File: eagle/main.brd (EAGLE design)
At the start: 98.7 x 90.2 mm, 31 parts, among them IC1 7805TV, U1 INA213AIDCKT, U2 LM1117MP-3.3, U3 INA213AIDCKT, U4 INA213AIDCKT

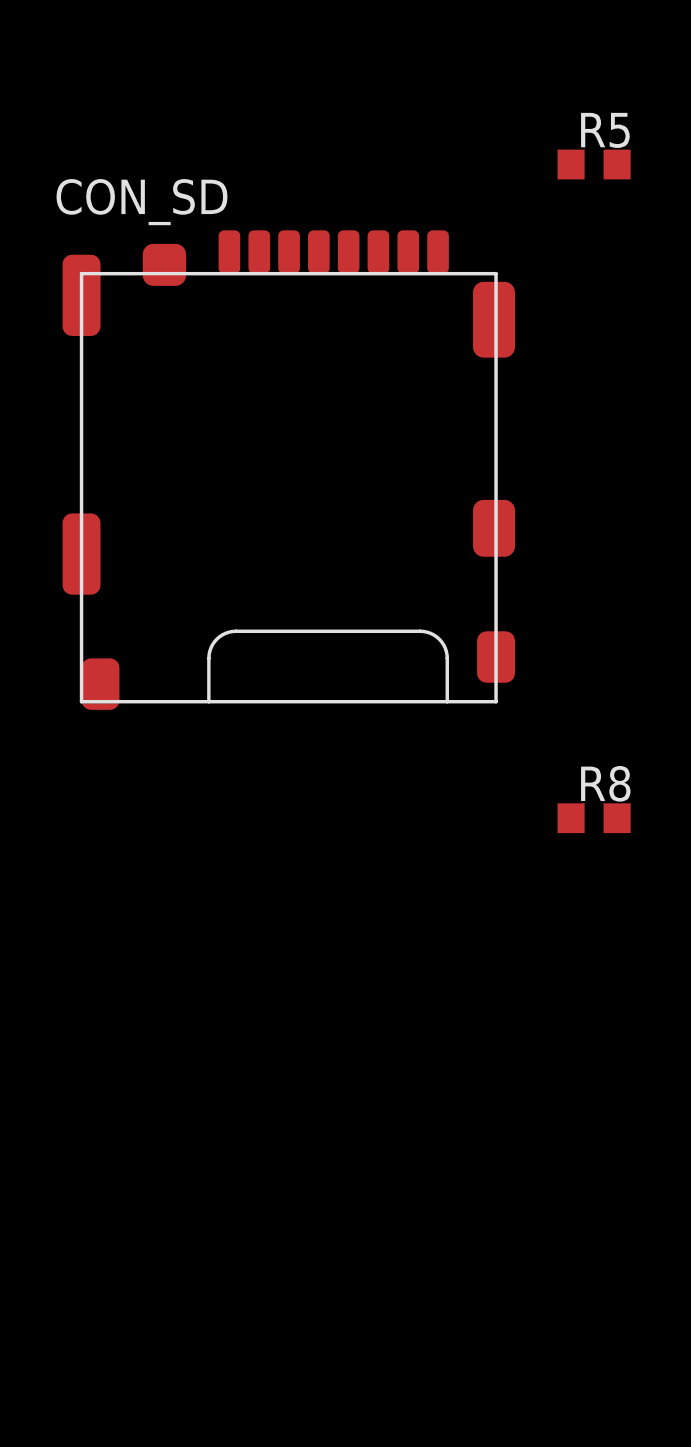
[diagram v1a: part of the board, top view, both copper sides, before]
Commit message: add Spansion flash memory
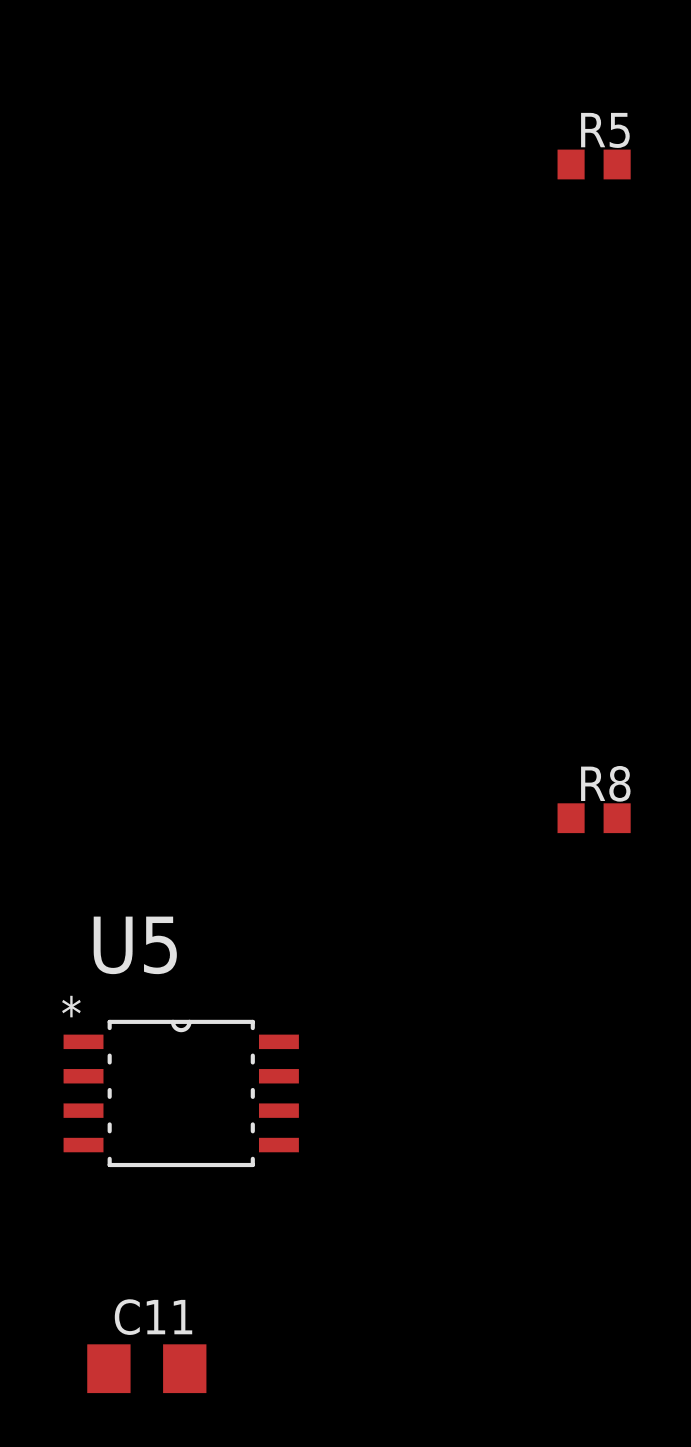
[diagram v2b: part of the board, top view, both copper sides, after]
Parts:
- removed CON_SD: MICROSD_SPI_MODE, con-molex-microsd:MICRO_SD_CONNECTOR
- added C11: 100n, rcl:C1206
- added U5: S25FL064K0SMFI011, Spansion_By_element14_Batch_1:SOIC127P800X215-8N
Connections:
- new net FLASH_CSN: U5.1
- new net FLASH_MISO: U5.2
- new net FLASH_MOSI: U5.5
- new net FLASH_SCK: U5.6
- net DC_3V3: now also C11.1, U5.8
- net GND: now also C11.2, U5.4
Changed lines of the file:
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@@
 <element name="C9" library="rcl" package="C1206" value="100n" x="-59.69" y="-68.58"/>
 <element name="C10" library="rcl" package="C1206" value="100n" x="-53.34" y="-68.58"/>
-<element name="CON_SD" library="con-molex-microsd" package="MICRO_SD_CONNECTOR" value="MICROSD_SPI_MODE" x="-81.28" y="-62.23"/>
+<element name="U5" library="Spansion_By_element14_Batch_1" package="SOIC127P800X215-8N" value="S25FL064K0SMFI011" x="-85.09" y="-85.09">
+<attribute name="PACKAGE" value="SOIC-8" x="-85.09" y="-85.09" size="1.778" layer="27" display="off"/>
+<attribute name="OC_NEWARK" value="27T2974" x="-85.09" y="-85.09" size="1.778" layer="27" display="off"/>
+<attribute name="MPN" value="S25FL064K0SMFI011" x="-85.09" y="-85.09" size="1.778" layer="27" display="off"/>
+<attribute name="SUPPLIER" value="SPANSION" x="-85.09" y="-85.09" size="1.778" layer="27" display="off"/>
+<attribute name="OC_FARNELL" value="1861631" x="-85.09" y="-85.09" size="1.778" layer="27" display="off"/>
+</element>
+<element name="C11" library="rcl" package="C1206" value="100n" x="-86.36" y="-95.25"/>
 </elements>
 <signals>
@@
 <contactref element="U4" pad="2"/>
 <contactref element="C10" pad="2"/>
-<wire x1="63.5" y1="78.74" x2="29.4386" y2="53.9496" width="0" layer="19" extent="1-1"/>
+<contactref element="U5" pad="4"/>
+<contactref element="C11" pad="2"/>
+<wire x1="-88.6968" y1="-86.995" x2="-84.96" y2="-95.25" width="0" layer="19" extent="1-1"/>
+<wire x1="-64.35" y1="-74.93" x2="-88.6968" y2="-86.995" width="0" layer="19" extent="1-1"/>
+<wire x1="-58.29" y1="-68.58" x2="-64.35" y2="-74.93" width="0" layer="19" extent="1-1"/>
+<wire x1="-51.94" y1="-68.58" x2="-58.29" y2="-68.58" width="0" layer="19" extent="1-1"/>
+<wire x1="-64.35" y1="-50.8" x2="-58.29" y2="-68.58" width="0" layer="19" extent="1-1"/>
+<wire x1="-58.29" y1="-44.45" x2="-64.35" y2="-50.8" width="0" layer="19" extent="1-1"/>
+<wire x1="-51.94" y1="-44.45" x2="-58.29" y2="-44.45" width="0" layer="19" extent="1-1"/>
+<wire x1="-65.81" y1="-25.4" x2="-58.29" y2="-44.45" width="0" layer="19" extent="1-1"/>
+<wire x1="-65.81" y1="-17.78" x2="-65.81" y2="-25.4" width="0" layer="19" extent="1-1"/>
+<wire x1="-56.92" y1="-10.16" x2="-65.81" y2="-17.78" width="0" layer="19" extent="1-1"/>
+<wire x1="-56.92" y1="-3.81" x2="-56.92" y2="-10.16" width="0" layer="19" extent="1-1"/>
+<wire x1="6.35" y1="17.78" x2="-56.92" y2="-3.81" width="0" layer="19" extent="1-1"/>
+<wire x1="6.35" y1="27.94" x2="6.35" y2="17.78" width="0" layer="19" extent="1-1"/>
+<wire x1="18.0086" y1="20.32" x2="6.35" y2="17.78" width="0" layer="19" extent="1-1"/>
+<wire x1="18.0086" y1="20.9804" x2="18.0086" y2="20.32" width="0" layer="19" extent="1-1"/>
+<wire x1="6.35" y1="43.18" x2="6.35" y2="27.94" width="0" layer="19" extent="1-1"/>
+<wire x1="6.35" y1="53.34" x2="6.35" y2="43.18" width="0" layer="19" extent="1-1"/>
+<wire x1="18.0086" y1="45.72" x2="6.35" y2="43.18" width="0" layer="19" extent="1-1"/>
+<wire x1="18.0086" y1="46.3804" x2="18.0086" y2="45.72" width="0" layer="19" extent="1-1"/>
+<wire x1="20.32" y1="57.15" x2="18.0086" y2="46.3804" width="0" layer="19" extent="1-1"/>
+<wire x1="29.4386" y1="53.9496" x2="20.32" y2="57.15" width="0" layer="19" extent="1-1"/>
+<wire x1="6.35" y1="68.58" x2="6.35" y2="53.34" width="0" layer="19" extent="1-1"/>
+<wire x1="6.35" y1="78.74" x2="6.35" y2="68.58" width="0" layer="19" extent="1-1"/>
+<wire x1="18.0086" y1="72.39" x2="6.35" y2="68.58" width="0" layer="19" extent="1-1"/>
+<wire x1="18.0086" y1="73.0504" x2="18.0086" y2="72.39" width="0" layer="19" extent="1-1"/>
+<wire x1="30.61" y1="73.66" x2="18.0086" y2="73.0504" width="0" layer="19" extent="1-1"/>
+<wire x1="-18.63" y1="74.93" x2="6.35" y2="78.74" width="0" layer="19" extent="1-1"/>
+<wire x1="-46.86" y1="73.66" x2="-18.63" y2="74.93" width="0" layer="19" extent="1-1"/>
+<wire x1="63.5" y1="78.74" x2="30.61" y2="73.66" width="0" layer="19" extent="1-1"/>
 <wire x1="71.12" y1="45.72" x2="63.5" y2="78.74" width="0" layer="19" extent="1-1"/>
-<wire x1="6.35" y1="78.74" x2="63.5" y2="78.74" width="0" layer="19" extent="1-1"/>
-<wire x1="6.35" y1="68.58" x2="6.35" y2="78.74" width="0" layer="19" extent="1-1"/>
-<wire x1="6.35" y1="53.34" x2="6.35" y2="68.58" width="0" layer="19" extent="1-1"/>
-<wire x1="6.35" y1="43.18" x2="6.35" y2="53.34" width="0" layer="19" extent="1-1"/>
-<wire x1="6.35" y1="27.94" x2="6.35" y2="43.18" width="0" layer="19" extent="1-1"/>
-<wire x1="6.35" y1="17.78" x2="6.35" y2="27.94" width="0" layer="19" extent="1-1"/>
-<wire x1="95.25" y1="66.04" x2="6.35" y2="17.78" width="0" layer="19" extent="1-1"/>
-<wire x1="-18.63" y1="74.93" x2="6.35" y2="78.74" width="0" layer="19" extent="1-1"/>
-<wire x1="18.0086" y1="20.9804" x2="-18.63" y2="74.93" width="0" layer="19" extent="1-1"/>
-<wire x1="18.0086" y1="20.32" x2="18.0086" y2="20.9804" width="0" layer="19" extent="1-1"/>
-<wire x1="20.32" y1="57.15" x2="18.0086" y2="20.32" width="0" layer="19" extent="1-1"/>
-<wire x1="30.61" y1="73.66" x2="20.32" y2="57.15" width="0" layer="19" extent="1-1"/>
-<wire x1="-46.86" y1="73.66" x2="30.61" y2="73.66" width="0" layer="19" extent="1-1"/>
-<wire x1="-56.92" y1="-3.81" x2="6.35" y2="17.78" width="0" layer="19" extent="1-1"/>
-<wire x1="-56.92" y1="-10.16" x2="-56.92" y2="-3.81" width="0" layer="19" extent="1-1"/>
-<wire x1="-65.81" y1="-17.78" x2="-56.92" y2="-10.16" width="0" layer="19" extent="1-1"/>
-<wire x1="-65.81" y1="-25.4" x2="-65.81" y2="-17.78" width="0" layer="19" extent="1-1"/>
-<wire x1="18.0086" y1="46.3804" x2="-65.81" y2="-25.4" width="0" layer="19" extent="1-1"/>
-<wire x1="18.0086" y1="45.72" x2="18.0086" y2="46.3804" width="0" layer="19" extent="1-1"/>
-<wire x1="-58.29" y1="-44.45" x2="18.0086" y2="45.72" width="0" layer="19" extent="1-1"/>
-<wire x1="-51.94" y1="-44.45" x2="-58.29" y2="-44.45" width="0" layer="19" extent="1-1"/>
-<wire x1="-64.35" y1="-50.8" x2="-58.29" y2="-44.45" width="0" layer="19" extent="1-1"/>
-<wire x1="18.0086" y1="73.0504" x2="-64.35" y2="-50.8" width="0" layer="19" extent="1-1"/>
-<wire x1="18.0086" y1="72.39" x2="18.0086" y2="73.0504" width="0" layer="19" extent="1-1"/>
-<wire x1="-58.29" y1="-68.58" x2="18.0086" y2="72.39" width="0" layer="19" extent="1-1"/>
-<wire x1="-51.94" y1="-68.58" x2="-58.29" y2="-68.58" width="0" layer="19" extent="1-1"/>
-<wire x1="-64.35" y1="-74.93" x2="-58.29" y2="-68.58" width="0" layer="19" extent="1-1"/>
+<wire x1="95.25" y1="66.04" x2="71.12" y2="45.72" width="0" layer="19" extent="1-1"/>
 </signal>
 <signal name="AGND">
@@
 <contactref element="U4" pad="3"/>
 <contactref element="C10" pad="1"/>
-<wire x1="18.0086" y1="19.6596" x2="34.0614" y2="53.9496" width="0" layer="19" extent="1-1"/>
-<wire x1="-49.66" y1="73.66" x2="18.0086" y2="19.6596" width="0" layer="19" extent="1-1"/>
-<wire x1="20.32" y1="52.07" x2="18.0086" y2="19.6596" width="0" layer="19" extent="1-1"/>
-<wire x1="-68.81" y1="-17.78" x2="20.32" y2="52.07" width="0" layer="19" extent="1-1"/>
-<wire x1="18.0086" y1="45.0596" x2="-68.81" y2="-17.78" width="0" layer="19" extent="1-1"/>
-<wire x1="-54.74" y1="-44.45" x2="18.0086" y2="45.0596" width="0" layer="19" extent="1-1"/>
-<wire x1="18.0086" y1="71.7296" x2="-54.74" y2="-44.45" width="0" layer="19" extent="1-1"/>
-<wire x1="-54.74" y1="-68.58" x2="18.0086" y2="71.7296" width="0" layer="19" extent="1-1"/>
+<wire x1="-54.74" y1="-44.45" x2="-54.74" y2="-68.58" width="0" layer="19" extent="1-1"/>
+<wire x1="-68.81" y1="-17.78" x2="-54.74" y2="-44.45" width="0" layer="19" extent="1-1"/>
+<wire x1="-49.66" y1="73.66" x2="-68.81" y2="-17.78" width="0" layer="19" extent="1-1"/>
+<wire x1="18.0086" y1="71.7296" x2="-49.66" y2="73.66" width="0" layer="19" extent="1-1"/>
+<wire x1="20.32" y1="52.07" x2="18.0086" y2="71.7296" width="0" layer="19" extent="1-1"/>
+<wire x1="18.0086" y1="45.0596" x2="20.32" y2="52.07" width="0" layer="19" extent="1-1"/>
+<wire x1="34.0614" y1="53.9496" x2="20.32" y2="52.07" width="0" layer="19" extent="1-1"/>
+<wire x1="18.0086" y1="19.6596" x2="18.0086" y2="45.0596" width="0" layer="19" extent="1-1"/>
 </signal>
 <signal name="PV_ISENSE">
@@
 <contactref element="U2" pad="2"/>
 <contactref element="C6" pad="+"/>
-<wire x1="31.75" y1="53.9496" x2="31.75" y2="60.3504" width="0" layer="19" extent="1-1"/>
-<wire x1="-68.81" y1="-25.4" x2="31.75" y2="53.9496" width="0" layer="19" extent="1-1"/>
+<contactref element="U5" pad="8"/>
+<contactref element="C11" pad="1"/>
+<wire x1="-81.4832" y1="-83.185" x2="-87.76" y2="-95.25" width="0" layer="19" extent="1-1"/>
+<wire x1="-68.81" y1="-25.4" x2="-81.4832" y2="-83.185" width="0" layer="19" extent="1-1"/>
+<wire x1="31.75" y1="53.9496" x2="-68.81" y2="-25.4" width="0" layer="19" extent="1-1"/>
+<wire x1="31.75" y1="60.3504" x2="31.75" y2="53.9496" width="0" layer="19" extent="1-1"/>
 </signal>
 <signal name="USB_5V">
@@
 <contactref element="U4" pad="6"/>
 </signal>
+<signal name="FLASH_SCK">
+<contactref element="U5" pad="6"/>
+</signal>
+<signal name="FLASH_MOSI">
+<contactref element="U5" pad="5"/>
+</signal>
+<signal name="FLASH_CSN">
+<contactref element="U5" pad="1"/>
+</signal>
+<signal name="FLASH_MISO">
+<contactref element="U5" pad="2"/>
+</signal>
 </signals>

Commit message: add dia
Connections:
- new net LOAD_GND: C7.2, CON_LOAD.P$3, CON_LOAD.P$4, R6.1
- new net PV_GND: C1.2, CON_PV.P$3, CON_PV.P$4, R3.1
- net GND: no longer C1.2, C7.2, CON_LOAD.P$3, CON_LOAD.P$4, CON_PV.P$3, CON_PV.P$4, R3.1, R6.1
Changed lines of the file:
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@@
 <contactref element="U$1" pad="GND1"/>
 <contactref element="CON_SPI" pad="1"/>
-<contactref element="CON_PV" pad="P$3"/>
-<contactref element="CON_LOAD" pad="P$3"/>
 <contactref element="CON_BAT" pad="P$3"/>
-<contactref element="R3" pad="1"/>
-<contactref element="C1" pad="2"/>
 <contactref element="U1" pad="1"/>
 <contactref element="U1" pad="2"/>
 <contactref element="C2" pad="2"/>
-<contactref element="CON_PV" pad="P$4"/>
-<contactref element="CON_LOAD" pad="P$4"/>
 <contactref element="CON_BAT" pad="P$4"/>
 <contactref element="IC1" pad="2"/>
@@
 <contactref element="C5" pad="-"/>
 <contactref element="C6" pad="-"/>
-<contactref element="R6" pad="1"/>
-<contactref element="C7" pad="2"/>
 <contactref element="U3" pad="1"/>
 <contactref element="U3" pad="2"/>
@@
 <wire x1="-58.29" y1="-68.58" x2="-64.35" y2="-74.93" width="0" layer="19" extent="1-1"/>
 <wire x1="-51.94" y1="-68.58" x2="-58.29" y2="-68.58" width="0" layer="19" extent="1-1"/>
-<wire x1="-64.35" y1="-50.8" x2="-58.29" y2="-68.58" width="0" layer="19" extent="1-1"/>
-<wire x1="-58.29" y1="-44.45" x2="-64.35" y2="-50.8" width="0" layer="19" extent="1-1"/>
-<wire x1="-51.94" y1="-44.45" x2="-58.29" y2="-44.45" width="0" layer="19" extent="1-1"/>
-<wire x1="-65.81" y1="-25.4" x2="-58.29" y2="-44.45" width="0" layer="19" extent="1-1"/>
+<wire x1="-51.94" y1="-44.45" x2="-51.94" y2="-68.58" width="0" layer="19" extent="1-1"/>
+<wire x1="-65.81" y1="-25.4" x2="-51.94" y2="-44.45" width="0" layer="19" extent="1-1"/>
 <wire x1="-65.81" y1="-17.78" x2="-65.81" y2="-25.4" width="0" layer="19" extent="1-1"/>
 <wire x1="-56.92" y1="-10.16" x2="-65.81" y2="-17.78" width="0" layer="19" extent="1-1"/>
 <wire x1="-56.92" y1="-3.81" x2="-56.92" y2="-10.16" width="0" layer="19" extent="1-1"/>
-<wire x1="6.35" y1="17.78" x2="-56.92" y2="-3.81" width="0" layer="19" extent="1-1"/>
-<wire x1="6.35" y1="27.94" x2="6.35" y2="17.78" width="0" layer="19" extent="1-1"/>
-<wire x1="18.0086" y1="20.32" x2="6.35" y2="17.78" width="0" layer="19" extent="1-1"/>
-<wire x1="18.0086" y1="20.9804" x2="18.0086" y2="20.32" width="0" layer="19" extent="1-1"/>
-<wire x1="6.35" y1="43.18" x2="6.35" y2="27.94" width="0" layer="19" extent="1-1"/>
-<wire x1="6.35" y1="53.34" x2="6.35" y2="43.18" width="0" layer="19" extent="1-1"/>
-<wire x1="18.0086" y1="45.72" x2="6.35" y2="43.18" width="0" layer="19" extent="1-1"/>
-<wire x1="18.0086" y1="46.3804" x2="18.0086" y2="45.72" width="0" layer="19" extent="1-1"/>
-<wire x1="20.32" y1="57.15" x2="18.0086" y2="46.3804" width="0" layer="19" extent="1-1"/>
-<wire x1="29.4386" y1="53.9496" x2="20.32" y2="57.15" width="0" layer="19" extent="1-1"/>
-<wire x1="6.35" y1="68.58" x2="6.35" y2="53.34" width="0" layer="19" extent="1-1"/>
-<wire x1="6.35" y1="78.74" x2="6.35" y2="68.58" width="0" layer="19" extent="1-1"/>
+<wire x1="-46.86" y1="73.66" x2="-56.92" y2="-3.81" width="0" layer="19" extent="1-1"/>
+<wire x1="6.35" y1="78.74" x2="-46.86" y2="73.66" width="0" layer="19" extent="1-1"/>
+<wire x1="6.35" y1="68.58" x2="6.35" y2="78.74" width="0" layer="19" extent="1-1"/>
 <wire x1="18.0086" y1="72.39" x2="6.35" y2="68.58" width="0" layer="19" extent="1-1"/>
 <wire x1="18.0086" y1="73.0504" x2="18.0086" y2="72.39" width="0" layer="19" extent="1-1"/>
-<wire x1="30.61" y1="73.66" x2="18.0086" y2="73.0504" width="0" layer="19" extent="1-1"/>
-<wire x1="-18.63" y1="74.93" x2="6.35" y2="78.74" width="0" layer="19" extent="1-1"/>
-<wire x1="-46.86" y1="73.66" x2="-18.63" y2="74.93" width="0" layer="19" extent="1-1"/>
-<wire x1="63.5" y1="78.74" x2="30.61" y2="73.66" width="0" layer="19" extent="1-1"/>
+<wire x1="20.32" y1="57.15" x2="18.0086" y2="72.39" width="0" layer="19" extent="1-1"/>
+<wire x1="29.4386" y1="53.9496" x2="20.32" y2="57.15" width="0" layer="19" extent="1-1"/>
+<wire x1="18.0086" y1="46.3804" x2="20.32" y2="57.15" width="0" layer="19" extent="1-1"/>
+<wire x1="18.0086" y1="45.72" x2="18.0086" y2="46.3804" width="0" layer="19" extent="1-1"/>
+<wire x1="18.0086" y1="20.9804" x2="18.0086" y2="45.72" width="0" layer="19" extent="1-1"/>
+<wire x1="18.0086" y1="20.32" x2="18.0086" y2="20.9804" width="0" layer="19" extent="1-1"/>
+<wire x1="63.5" y1="78.74" x2="29.4386" y2="53.9496" width="0" layer="19" extent="1-1"/>
 <wire x1="71.12" y1="45.72" x2="63.5" y2="78.74" width="0" layer="19" extent="1-1"/>
 <wire x1="95.25" y1="66.04" x2="71.12" y2="45.72" width="0" layer="19" extent="1-1"/>
@@
 <contactref element="U5" pad="2"/>
 </signal>
+<signal name="LOAD_GND">
+<contactref element="CON_LOAD" pad="P$3"/>
+<contactref element="CON_LOAD" pad="P$4"/>
+<contactref element="R6" pad="1"/>
+<contactref element="C7" pad="2"/>
+<wire x1="-58.29" y1="-44.45" x2="-64.35" y2="-50.8" width="0" layer="19" extent="1-1"/>
+<wire x1="6.35" y1="43.18" x2="-58.29" y2="-44.45" width="0" layer="19" extent="1-1"/>
+<wire x1="6.35" y1="53.34" x2="6.35" y2="43.18" width="0" layer="19" extent="1-1"/>
+</signal>
+<signal name="PV_GND">
+<contactref element="CON_PV" pad="P$3"/>
+<contactref element="CON_PV" pad="P$4"/>
+<contactref element="R3" pad="1"/>
+<contactref element="C1" pad="2"/>
+<wire x1="-18.63" y1="74.93" x2="30.61" y2="73.66" width="0" layer="19" extent="1-1"/>
+<wire x1="6.35" y1="27.94" x2="30.61" y2="73.66" width="0" layer="19" extent="1-1"/>
+<wire x1="6.35" y1="17.78" x2="6.35" y2="27.94" width="0" layer="19" extent="1-1"/>
+</signal>
 </signals>

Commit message: add TI library
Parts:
- removed C10, C9: 100n, rcl:C1206
- removed CON_SPI: (no value), con-lstb:MA06-1
- removed R7: 0.002, resistor:R2512
- removed R8: 470K, rcl:R0603
- removed R9: 20K, rcl:R0603
- removed U4: INA213AIDCKT, TI-INA213AIDCKT:SOT65P210X110-6N
- added C12: 100n, rcl:C1206
- added CON_GPIO: (no value), con-lstb:MA05-2
- added R10, R12: 10K, rcl:R0603
- added R11: 100K, rcl:R0603
- added U6, U8: INA146UA, Texas Instruments_By_element14_Batch_1:SOIC127P600X175-8N
- added U7: INA213AIDCKT, TI-INA213AIDCKT:SOT65P210X110-6N
- R2: value 470K -> 68K
- R3: value 20K -> 100K
- R5: value 470K -> 0.002; device rcl:R0603 -> resistor:R2512
- R6: value 20K -> 68K
- moved C1 248.8 mm to (-77.5, -151.1)
- moved R6 107.4 mm to (-76.2, -157.5)
- moved C7 107.3 mm to (-71.1, -151.1)
- moved R5 101.5 mm to (-85.1, -151.1)
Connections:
- removed net BAT_5V: C4.+, IC1.3, JP1.3
- removed net LOAD_VSENSE: C7.1, R5.1, R6.2
- removed net SPI_CS: CON_SPI.3
- removed net SPI_IRQ: CON_SPI.2
- removed net SPI_MISO: CON_SPI.6
- removed net SPI_MOSI: CON_SPI.5
- removed net SPI_SCK: CON_SPI.4
- new net BAT_GND: C3.-, CON_BAT.P$3, CON_BAT.P$4, IC1.1, R11.1
- new net BAT_VDIV: R11.2, R6.1, U8.2
- new net GPIO_0: CON_GPIO.5
- new net GPIO_1: CON_GPIO.6
- new net GPIO_2: CON_GPIO.7
- new net GPIO_3: CON_GPIO.8
- new net GPIO_4: CON_GPIO.9
- new net GPIO_5: CON_GPIO.10
- new net N$1: R12.1, U8.6
- new net N$2: R10.1, U6.6
- new net N$4: IC1.2
- new net PV_VDIV: R2.1, R3.2, U6.2
- net BAT_IN: now also C4.+, JP1.3, R5.2, U7.4; no longer IC1.1, R7.2, U4.4
- net BAT_ISENSE: now also U7.6; no longer U4.6
- net BAT_OUT: now also R5.1, R6.2, U7.5, U8.3; no longer R7.1, R8.2, U4.5
- net BAT_VSENSE: now also R12.2, U8.5; no longer C9.1, R8.1, R9.2
- net DC_3V3: now also CON_GPIO.3
- net DC_5V: now also C1.1, C12.1, C7.1, CON_GPIO.4, U6.7, U7.3, U8.7; no longer C10.1, U4.3
- net GND: now also C1.2, C12.2, C7.2, CON_GPIO.1, CON_GPIO.2, IC1.3, U6.1, U6.4, U7.1, U7.2, U8.1, U8.4; no longer C10.2, C3.-, C9.2, CON_BAT.P$3, CON_BAT.P$4, CON_SPI.1, IC1.2, R9.1, U4.1, U4.2
- net LOAD_GND: no longer C7.2, R6.1
- net LOAD_OUT: no longer R5.2
- net PV_GND: no longer C1.2
- net PV_OUT: now also U6.3
- net PV_VSENSE: now also R10.2, U6.5; no longer C1.1, R2.1, R3.2
